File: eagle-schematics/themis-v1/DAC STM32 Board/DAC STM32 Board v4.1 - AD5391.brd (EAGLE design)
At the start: 100 x 80 mm, 36 parts, among them IC1 MCP23017SO, U1 ANALOG_DEVICES_AD5391BSTZ-3AN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

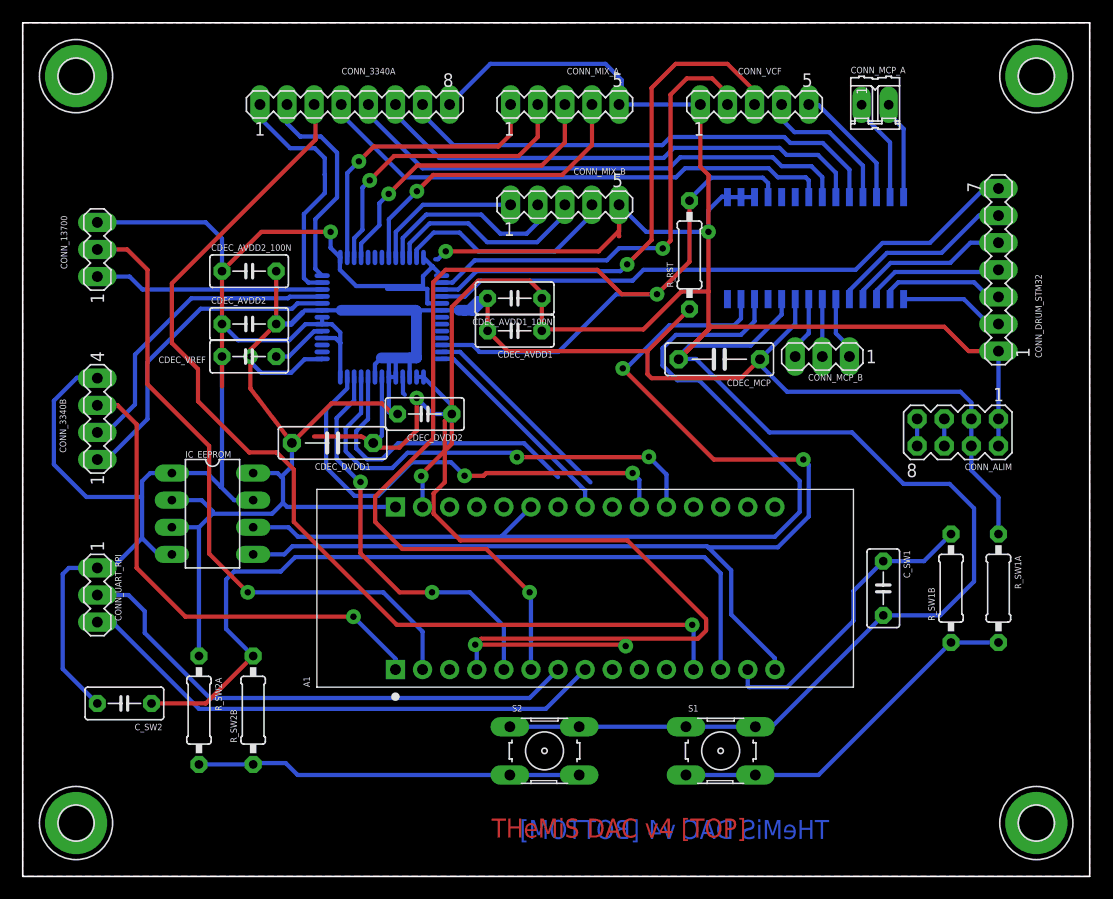
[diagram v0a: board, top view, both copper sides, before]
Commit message: Added new schematic for HP-LP-BP filter
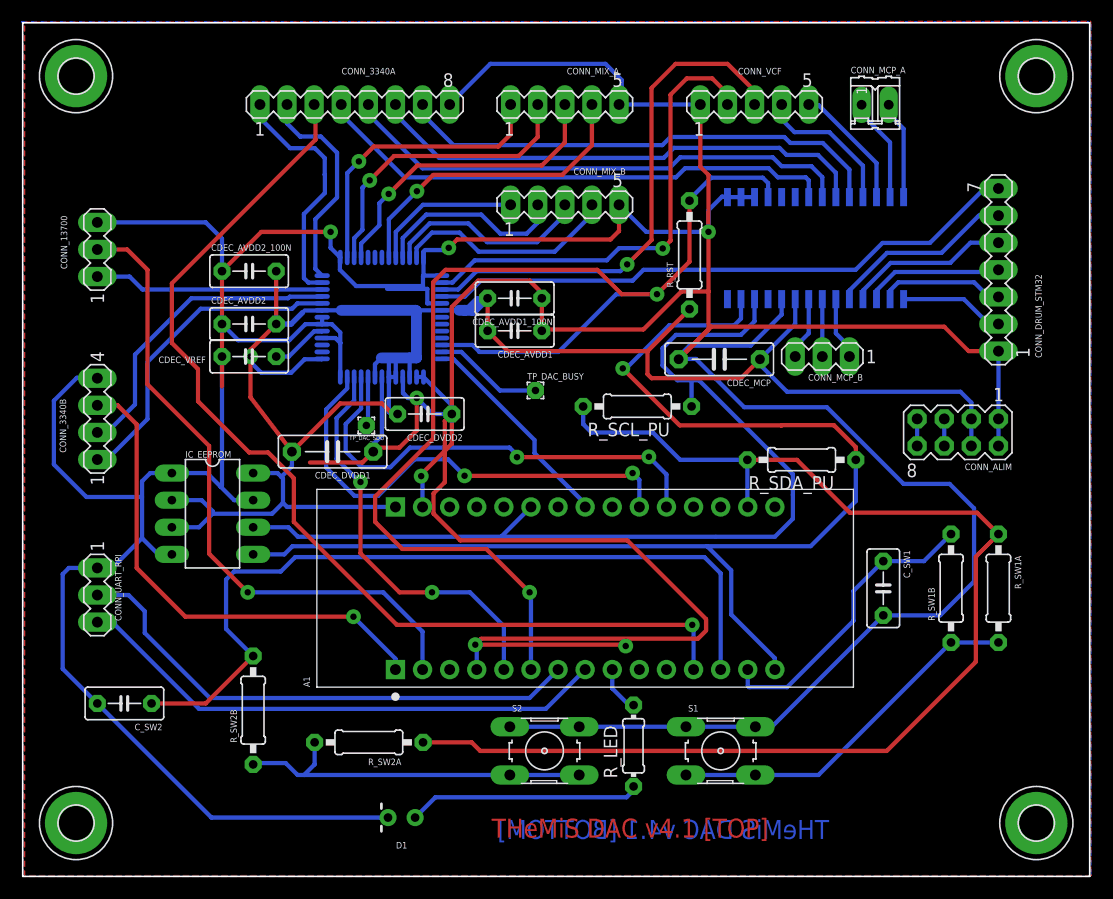
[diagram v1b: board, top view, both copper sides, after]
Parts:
- added D1: (no value), SparkFun-LED:LED_3MM-NS
- added R_LED: 330, 6P1_EVB:0204/7
- added R_SCL_PU, R_SDA_PU: 1k, 6P1_EVB:0207/10
- added TP_DAC_BUSY, TP_DAC_SDO: PAD-TESTPOINT, ee2parts:1,6/0,8
- moved R_SW2A 16.2 mm to (32.4, 12.6), turned to 180 degrees
- moved CDEC_DVDD1 0.81 mm to (29.0, 39.8)
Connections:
- removed net DAC_BUSY: A1.4.9, U1.38
- new net LED: A1.3.9, R_LED.2
- new net N$1: TP_DAC_BUSY.1, U1.38
- new net N$4: D1.A, R_LED.1
- net 3V3: now also R_SCL_PU.2, R_SDA_PU.2, R_SW1A.1, R_SW2A.1
- net 5V: no longer R_SW1A.1, R_SW2A.1
- net GND: now also D1.K
- net SCL: now also R_SCL_PU.1
- net SDA: now also R_SDA_PU.1
- net SPI_MISO: now also TP_DAC_SDO.1; no longer A1.4.7
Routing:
- net 3V3: track 0.00 -> 117.8 mm
- net GND: track 554.9 -> 587.9 mm
- net SPI_MISO: track 28.4 -> 4.60 mm
- net N$4: track 0.00 -> 21.9 mm
- net 5V: track 211.7 -> 190.6 mm
- net DAC_BUSY: track 19.0 -> 0.00 mm
- net N$1: track 0.00 -> 10.3 mm
- net SDA: track 108.6 -> 117.7 mm, vias 2 -> 1
- net LED: track 0.00 -> 4.41 mm
- net SCL: track 90.1 -> 92.1 mm
- net N$7: track 36.2 -> 34.5 mm
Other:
- board text added: "THeMiS DAC v4.1 [BOTTOM]"
- board text added: "THeMiS DAC v4.1 [TOP]"
- board text removed: "THeMiS DAC v4 [BOTTOM]"
- board text removed: "THeMiS DAC v4 [TOP]"
